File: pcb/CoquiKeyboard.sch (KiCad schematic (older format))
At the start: 116 parts, among them SW1 SW_Push, U1 ATmega32U4-MU, Y1 16MHz

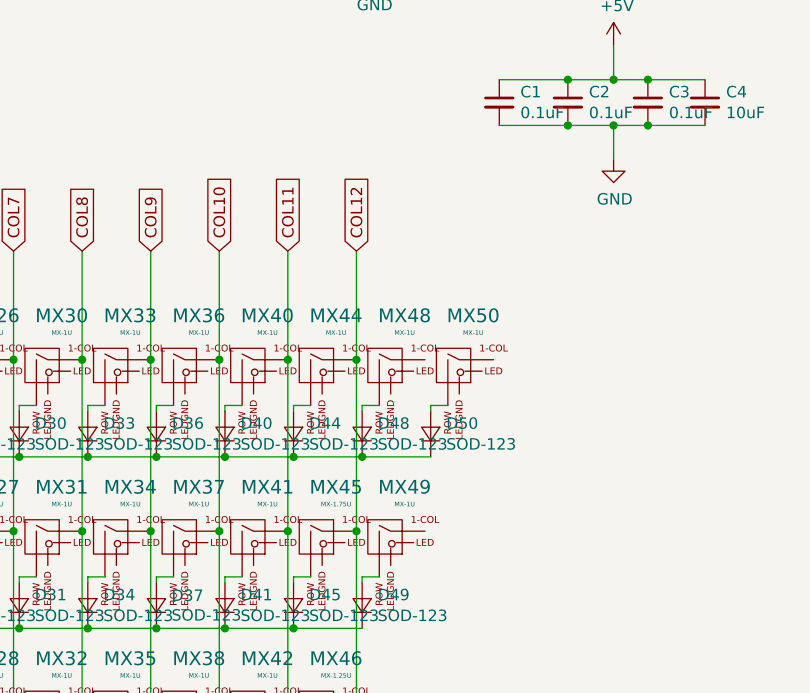
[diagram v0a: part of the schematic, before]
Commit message: fix keysize error
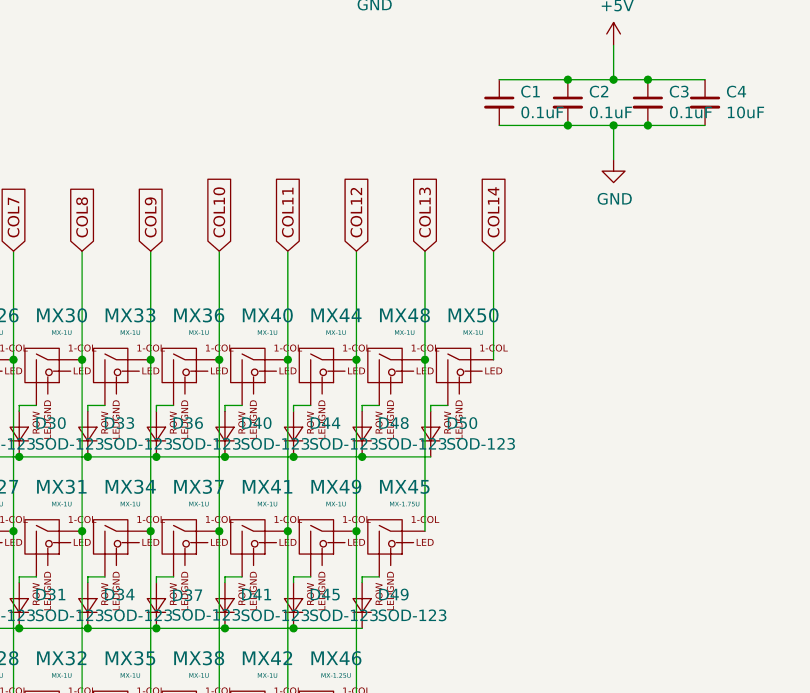
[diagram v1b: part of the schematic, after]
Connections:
- net labels added: COL13, COL14
- wire segments 248 -> 251
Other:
- moved on the sheet: MX45, MX49
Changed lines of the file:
@@
 L MX_Alps_Hybrids:MX-1U MX49
 U 1 1 5CEFDBC9
-P 5200 5100
-F 0 "MX49" H 5286 5317 60  0000 C CNN
-F 1 "MX-1U" H 5286 5243 20  0000 C CNN
-F 2 "MX_Alps_Hybrid:MX-1U" H 5175 5075 60  0001 C CNN
-F 3 "" H 5175 5075 60  0001 C CNN
-	1    5200 5100
+P 4900 5100
+F 0 "MX49" H 4986 5317 60  0000 C CNN
+F 1 "MX-1U" H 4986 5243 20  0000 C CNN
+F 2 "MX_Alps_Hybrid:MX-1U" H 4875 5075 60  0001 C CNN
+F 3 "" H 4875 5075 60  0001 C CNN
+	1    4900 5100
 	1    0    0    -1
 $EndComp
@@
 L MX_Alps_Hybrids:MX-1.75U MX45
 U 1 1 5CF7D59E
-P 4900 5100
-F 0 "MX45" H 4986 5317 60  0000 C CNN
-F 1 "MX-1.75U" H 4986 5243 20  0000 C CNN
-F 2 "MX_Alps_Hybrid:MX-1.75U" H 4875 5075 60  0001 C CNN
-F 3 "" H 4875 5075 60  0001 C CNN
-	1    4900 5100
+P 5200 5100
+F 0 "MX45" H 5286 5317 60  0000 C CNN
+F 1 "MX-1.75U" H 5286 5243 20  0000 C CNN
+F 2 "MX_Alps_Hybrid:MX-1.75U" H 5175 5075 60  0001 C CNN
+F 3 "" H 5175 5075 60  0001 C CNN
+	1    5200 5100
 	1    0    0    -1
 $EndComp
@@
 Wire Wire Line
 	3575 5825 3575 6550
+Wire Wire Line
+	5375 4325 5375 5075
+Wire Wire Line
+	5675 4325 5675 3850
+Text GLabel 5375 3850 1    50   Input ~ 0
+COL13
+Text GLabel 5675 3850 1    50   Input ~ 0
+COL14
+Wire Wire Line
+	5375 3850 5375 4325
+Connection ~ 5375 4325
 $EndSCHEMATC

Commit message: fix positioning of switches
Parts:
- added D?: SOD-123, Diode_SMD:D_SOD-123, symbol Device:D_Small
- added MX?: MX-1U, MX_Alps_Hybrid:MX-1U, symbol MX_Alps_Hybrids:MX-1U
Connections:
- wire segments 251 -> 252
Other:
- moved on the sheet: D10, D14, D18, D19, D22, D25, D26, D29, D32, D35, D38, D42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

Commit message: arrange switches to keyboard layout
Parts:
- removed D45: SOD-123, Diode_SMD:D_SOD-123, symbol Device:D_Small
- removed MX3: MX-1.5U, MX_Alps_Hybrid:MX-1.5U, symbol MX_Alps_Hybrids:MX-1.5U
- removed MX49: MX-1U, MX_Alps_Hybrid:MX-1U, symbol MX_Alps_Hybrids:MX-1U
- added MX3: MX-1.75U, MX_Alps_Hybrid:MX-1.75U, symbol MX_Alps_Hybrids:MX-1.75U
- U1: footprint Package_QFP:LQFP-44_10x10mm_P0.8mm -> Package_QFP:TQFP-48-1EP_7x7mm_P0.5mm_EP3.5x3.5mm
- gave numbers to parts that had none: 2
- renumbered D11 to D10, D12 to D11, D13 to D12, D10 to D13, D15 to D14, D16 to D15, D17 to D16, D14 to D17, D20 to D18, D21 to D19, D18 to D20, D19 to D21, D23 to D22, D24 to D23, D22 to D24, D27 to D25, D28 to D26, D25 to D27, D30 to D28, D31 to D29, D29 to D30, D26 to D31, D33 to D32, D34 to D33, D32 to D34, D36 to D35, D37 to D36, D35 to D37, D39 to D38, D40 to D39, D41 to D40, D38 to D41, D43 to D42, D44 to D43, D42 to D45, D47 to D46, D48 to D47, D49 to D48, D46 to D49, D7 to D6, D8 to D7, D9 to D8, D6 to D9, MX11 to MX10, MX12 to MX11, MX13 to MX12, MX10 to MX13, MX15 to MX14, MX16 to MX15, MX17 to MX16, MX14 to MX17, MX20 to MX18, MX21 to MX19, MX18 to MX20, MX19 to MX21, MX23 to MX22, MX24 to MX23, MX22 to MX24, MX26 to MX25, MX27 to MX26, MX25 to MX27, MX30 to MX28, MX31 to MX29, MX28 to MX30, MX29 to MX31, MX33 to MX32, MX34 to MX33, MX32 to MX34, MX36 to MX35, MX37 to MX36, MX35 to MX37, MX39 to MX38, MX40 to MX39, MX41 to MX40, MX38 to MX41, MX43 to MX42, MX44 to MX43, MX42 to MX45, MX47 to MX46, MX48 to MX47, MX45 to MX48, MX46 to MX49, MX7 to MX6, MX8 to MX7, MX9 to MX8, MX6 to MX9
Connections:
- wire segments 252 -> 250

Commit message: clean up ratsnet
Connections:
- net COL3: no longer MX14.1 (COL)
- net COL4: now also MX14.1 (COL), MX17.1 (COL); no longer D18.2 (A)
- net ROW0: now also D18.1 (K); no longer D19.1 (K)
- net ROW1: now also D19.1 (K); no longer D18.1 (K), MX17.1 (COL)
- net at MX18.2 (ROW): now also D18.2 (A); no longer D19.2 (A)
- net at MX19.2 (ROW): now also D19.2 (A)
- net at MX40.2 (ROW): no longer D40.2 (A)
- net at MX14.2 (ROW): no longer D14.2 (A)
- net at MX21.2 (ROW): no longer D21.2 (A)
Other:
- moved on the sheet: C1, C2, C3, C4, C5, C6, C7, D1, D10, D11, D12, D13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

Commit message: updated files
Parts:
- removed MX14, MX2, MX38, MX6: MX-1.25U, MX_Alps_Hybrid:MX-1.25U, symbol MX_Alps_Hybrids:MX-1.25U
- removed MX15, MX16, MX28, MX29, MX30, MX42, MX43, MX45, MX47, MX50: MX-1U, MX_Alps_Hybrid:MX-1U, symbol MX_Alps_Hybrids:MX-1U
- removed MX21: MX-2.25U, MX_Alps_Hybrid:MX-2.25U, symbol MX_Alps_Hybrids:MX-2.25U
- removed MX3, MX48: MX-1.75U, MX_Alps_Hybrid:MX-1.75U, symbol MX_Alps_Hybrids:MX-1.75U
- removed MX31: MX-2.75U, MX_Alps_Hybrid:MX-2.75U, symbol MX_Alps_Hybrids:MX-2.75U
- removed U1: ATmega32U4-MU, Package_QFP:TQFP-48-1EP_7x7mm_P0.5mm_EP3.5x3.5mm, symbol MCU_Microchip_ATmega:ATmega32U4-MU
- added D44, D52, D53, D54: D, Diode_SMD:D_SOD-123, symbol Device:D_Small
- added MX14, MX2, MX21, MX3, MX31, MX38, MX44, MX52, MX53, MX6: MX-1U, MX_Alps_Hybrid:MXOnly-1U-NoLED, symbol MX_Alps_Hybrids:MX-1U
- added MX15, MX29, MX42-1, MX43, MX54: MX-1U, MX_Alps_Hybrid:MXOnly-1U-NoLED, symbol MX_Alps_Hybrids:MX-1U-FLIPPED
- added MX16, MX41-1, MX45, MX50: MX-1.25U, MX_Alps_Hybrid:MXOnly-1.25U-NoLED, symbol MX_Alps_Hybrids:MX-1.25U
- added MX28, MX30: MX-1.75U, MX_Alps_Hybrid:MXOnly-1.75U-NoLED, symbol MX_Alps_Hybrids:MX-1.75U
- added MX42: MX-1.25U, MX_Alps_Hybrid:MXOnly-1.25U-NoLED, symbol MX_Alps_Hybrids:MX-1.25U-FLIPPED
- added MX47: MX-2.25U, MX_Alps_Hybrid:MXOnly-2.25U-ReversedStabilizers-NoLED, symbol MX_Alps_Hybrids:MX-2.25U
- added MX48: MX-2.75U, MX_Alps_Hybrid:MXOnly-2.75U-ReversedStabilizers-NoLED, symbol MX_Alps_Hybrids:MX-2.75U
- added U1: ATmega32U4-AU, Package_QFP:TQFP-44_10x10mm_P0.8mm, symbol MCU_Microchip_ATmega:ATmega32U4-AU
- D1, D10, D11, D12, D13, D14, D15, D16, D17, D18, D19, D2, D20, D21, D22, D23, D24, D25, D26, D27, D28, D29, D3, D30, D31, D32, D33, D34, D35, D36, D37, D38, D39, D4, D40, D41, D42, D43, D45, D46, D47, D48, D49, D5, D50, D51, D6, D7, D8, D9: value SOD-123 -> D
- MX1, MX10, MX11, MX12, MX13, MX17, MX18, MX19, MX20, MX22, MX23, MX24, MX25, MX26, MX27, MX32, MX33, MX34, MX35, MX36, MX37, MX39, MX4, MX40, MX41, MX5, MX51, MX7, MX8, MX9: footprint MX_Alps_Hybrid:MX-1U -> MX_Alps_Hybrid:MXOnly-1U-NoLED
- MX46, MX49: footprint MX_Alps_Hybrid:MX-1.25U -> MX_Alps_Hybrid:MXOnly-1.25U-NoLED
- SW1: symbol Switch:SW_Push -> CoquiKeyboard-rescue:SW_Push-Switch
- USB1: value Molex-0548190589 -> USB Mini; footprint random-keyboard-parts:Molex-0548190589 -> local:USB-Mini-B_ LCSC-C46398; symbol random-keyboard-parts:Molex-0548190589 -> CoquiKeyboard-rescue:Molex-0548190589-random-keyboard-parts
- Y1: symbol Device:Crystal_GND24_Small -> CoquiKeyboard-rescue:Crystal_GND24_Small-Device
- renumbered R3 to R1, R1 to R3
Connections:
- net COL12 is gone; now on net colD: MX46.1 (COL)
- net +5V: now also U1.14 (VCC), U1.2 (UVCC), U1.24 (AVCC), U1.34 (VCC), U1.44 (AVCC), U1.7 (VBUS)
- net GND: now also USB1.6 (SHIELD), U1.15 (GND), U1.23 (GND), U1.35 (GND), U1.43 (GND), U1.5 (UGND)
- net at R1.2, SW1.2: now also U1.13 (~RESET)
- net XT2: now reaches C6.1, Y1.3
- net XT2: now also U1.16 (XTAL2)
- net XT1: now reaches C5.1, Y1.1
- net XT1: now also U1.17 (XTAL1)
- net MCU_D-: now reaches R3.1
- net MCU_D-: now also U1.3 (D-)
- net at R4.2: now also U1.33 (~HWB~/PE2)
- net MCU_D+: now reaches R2.1
- net MCU_D+: now also U1.4 (D+)
- net at C7.1: now also U1.6 (UCAP)
- net at D15.2 (A): now also MX15.1 (ROW)
- net at D28.2 (A): now also MX28.2 (ROW)
- net at D43.2 (A): now also MX43.1 (ROW)
- net at D47.2 (A): now also MX47.2 (ROW)
- net at D50.2 (A): now also MX50.2 (ROW)
- net at D16.2 (A): now also MX16.2 (ROW)
- net at D29.2 (A): now also MX29.1 (ROW)
- net at MX40.2 (ROW): now also D40.2 (A)
- net at D30.2 (A): now also MX30.2 (ROW)
- net at D41.2 (A), MX41.2 (ROW): now also MX41-1.2 (ROW)
- net at MX41.3 (LED): now also MX41-1.3 (LED)
- net at MX41.4 (LEDGND): now also MX41-1.4 (LEDGND)
- net at D45.2 (A): now also MX45.2 (ROW)
- net at D2.2 (A): now also MX2.2 (ROW)
- net at D48.2 (A): now also MX48.2 (ROW)
- net at D6.2 (A): now also MX6.2 (ROW)
- net at D31.2 (A): now also MX31.2 (ROW)
- net at D38.2 (A): now also MX38.2 (ROW)
- net at D42.2 (A): now also MX42-1.1 (ROW), MX42.1 (ROW)
- net at D3.2 (A): now also MX3.2 (ROW)
- net at D14.2 (A): now also MX14.2 (ROW)
- net at D21.2 (A): now also MX21.2 (ROW)
- net COL0 renamed colA
- net colA: now also MX16.1 (COL), MX30.1 (COL), MX44.1 (COL), U1.31 (PC6)
- net COL1 renamed colD
- net colD: now also MX19.1 (COL), MX33.1 (COL), U1.29 (PB5); no longer MX5.1 (COL)
- removed net COL10: MX35.1 (COL), MX36.1 (COL), MX37.1 (COL)
- removed net COL11: MX39.1 (COL), MX40.1 (COL), MX41.1 (COL)
- net COL13 renamed colJ
- net colJ: now also MX10.1 (COL), MX25.1 (COL), MX39.1 (COL), U1.26 (PD6)
- net COL14 renamed colL
- net colL: now also MX12.1 (COL), MX27.1 (COL), MX41.1 (COL), MX41-1.1 (COL), U1.22 (PD5)
- removed net COL2: MX10.1 (COL), MX7.1 (COL), MX8.1 (COL), MX9.1 (COL)
- removed net COL3: MX11.1 (COL), MX12.1 (COL), MX13.1 (COL)
- net COL4 renamed colB
- net colB: now also MX2.1 (COL), MX31.1 (COL), MX45.1 (COL), U1.30 (PB6)
- removed net COL5: MX18.1 (COL), MX19.1 (COL), MX20.1 (COL)
- removed net COL6: MX22.1 (COL), MX23.1 (COL), MX24.1 (COL)
- removed net COL7: MX25.1 (COL), MX26.1 (COL), MX27.1 (COL)
- removed net COL9: MX32.1 (COL), MX33.1 (COL), MX34.1 (COL)
- removed net ROW0: D1.1 (K), D11.1 (K), D15.1 (K), D18.1 (K), D22.1 (K), D25.1 (K), D28.1 (K), D32.1 (K), D35.1 (K), D39.1 (K), D4.1 (K), D43.1 (K), D47.1 (K), D50.1 (K), D7.1 (K)
- removed net ROW1: D12.1 (K), D16.1 (K), D19.1 (K), D2.1 (K), D23.1 (K), D26.1 (K), D29.1 (K), D33.1 (K), D36.1 (K), D40.1 (K), D48.1 (K), D5.1 (K), D51.1 (K), D8.1 (K)
- removed net ROW2: D13.1 (K), D17.1 (K), D20.1 (K), D24.1 (K), D27.1 (K), D3.1 (K), D30.1 (K), D34.1 (K), D37.1 (K), D41.1 (K), D45.1 (K), D49.1 (K), D9.1 (K)
- removed net ROW3: D10.1 (K), D14.1 (K), D21.1 (K), D31.1 (K), D38.1 (K), D42.1 (K), D46.1 (K), D6.1 (K)
- new net: MX42-1.3 (LED), MX42.3 (LED)
- new net: MX42-1.4 (LEDGND), MX42.4 (LEDGND)
- new net: D44.2 (A), MX44.2 (ROW)
- new net: D52.2 (A), MX52.2 (ROW)
- new net: D53.2 (A), MX53.2 (ROW)
- new net: D54.2 (A), MX54.1 (ROW)
- new net colC: MX18.1 (COL), MX3.1 (COL), MX32.1 (COL), U1.40 (PF1)
- new net colE: MX20.1 (COL), MX34.1 (COL), MX47.1 (COL), MX5.1 (COL), U1.28 (PB4)
- new net colF: MX21.1 (COL), MX35.1 (COL), MX6.1 (COL), U1.39 (PF4)
- new net colG: MX22.1 (COL), MX36.1 (COL), MX7.1 (COL), U1.38 (PF5)
- new net colH: MX23.1 (COL), MX37.1 (COL), MX48.1 (COL), MX8.1 (COL), U1.27 (PD7)
- new net colI: MX24.1 (COL), MX38.1 (COL), MX9.1 (COL), U1.37 (PF6)
- new net colK: MX11.1 (COL), MX26.1 (COL), MX40.1 (COL), MX50.1 (COL), U1.25 (PD4)
- new net colM: MX13.1 (COL), MX28.1 (COL), MX52.1 (COL), U1.21 (PD3)
- new net colN: MX14.1 (COL), MX42-1.2 (COL), MX42.2 (COL), MX53.1 (COL), U1.20 (PD2)
- new net colO: MX15.2 (COL), MX29.2 (COL), MX43.2 (COL), MX54.2 (COL), U1.18 (PD0)
- new net row0: D1.1 (K), D10.1 (K), D11.1 (K), D12.1 (K), D13.1 (K), D14.1 (K), D15.1 (K), D2.1 (K), D3.1 (K), D4.1 (K), D5.1 (K), D6.1 (K), D7.1 (K), D8.1 (K), D9.1 (K), U1.8 (PB0)
- new net row1: D16.1 (K), D17.1 (K), D18.1 (K), D19.1 (K), D20.1 (K), D21.1 (K), D22.1 (K), D23.1 (K), D24.1 (K), D25.1 (K), D26.1 (K), D27.1 (K), D28.1 (K), D29.1 (K), U1.41 (PF0)
- new net row2: D30.1 (K), D31.1 (K), D32.1 (K), D33.1 (K), D34.1 (K), D35.1 (K), D36.1 (K), D37.1 (K), D38.1 (K), D39.1 (K), D40.1 (K), D41.1 (K), D42.1 (K), D43.1 (K), U1.32 (PC7)
- new net row3: D44.1 (K), D45.1 (K), D46.1 (K), D47.1 (K), D48.1 (K), D49.1 (K), D50.1 (K), D51.1 (K), D52.1 (K), D53.1 (K), D54.1 (K), U1.19 (PD1)
- no-connect marks 0 -> 116
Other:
- moved on the sheet: C1, C2, C3, C4, F1, USB1
